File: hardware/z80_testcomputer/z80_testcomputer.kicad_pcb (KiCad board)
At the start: 2 copper layers, 95 x 100 mm, 16 parts, among them J1 Conn_02x15_Odd_Even, J2 Conn_02x15_Odd_Even, U1 Z84C000XVEG, U2 SRAM_512K8B_DIP_SOP_SOJ

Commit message: added EEPROM, experimenting with packages
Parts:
- added C5: 100n, SquantorRcl:C_0805+0603, F.Cu at (225.4, 145.7)
- added C6: 1u, SquantorRcl:C_0805+0603, F.Cu at (243.8, 103.5)
- added U3: EEPROM_512K8B_DIP, Package_DIP:DIP-32_W15.24mm, F.Cu at (224.7, 104.0)
- U2: footprint Package_SO:SSOP-32_11.305x20.495mm_P1.27mm -> Package_DIP:DIP-32_W15.24mm
- moved U2 96.5 mm to (245.0, 133.1)
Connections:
- U2 pad 1: (no net) -> /A17
- U2 pad 2: (no net) -> /A16
- U2 pad 30: (no net) -> /A18
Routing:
- net /!WR: track 62.8 -> 0.00 mm
- net /!BUSACK: track 62.8 -> 0.00 mm
- net /!WAIT: track 62.8 -> 0.00 mm
- net /!RD: track 62.8 -> 0.00 mm
- net /!NMI: track 62.0 -> 0.00 mm
- net /!HALT: track 61.9 -> 0.00 mm
- net /!MREQ: track 61.6 -> 0.00 mm
- net /!IORQ: track 61.6 -> 0.00 mm

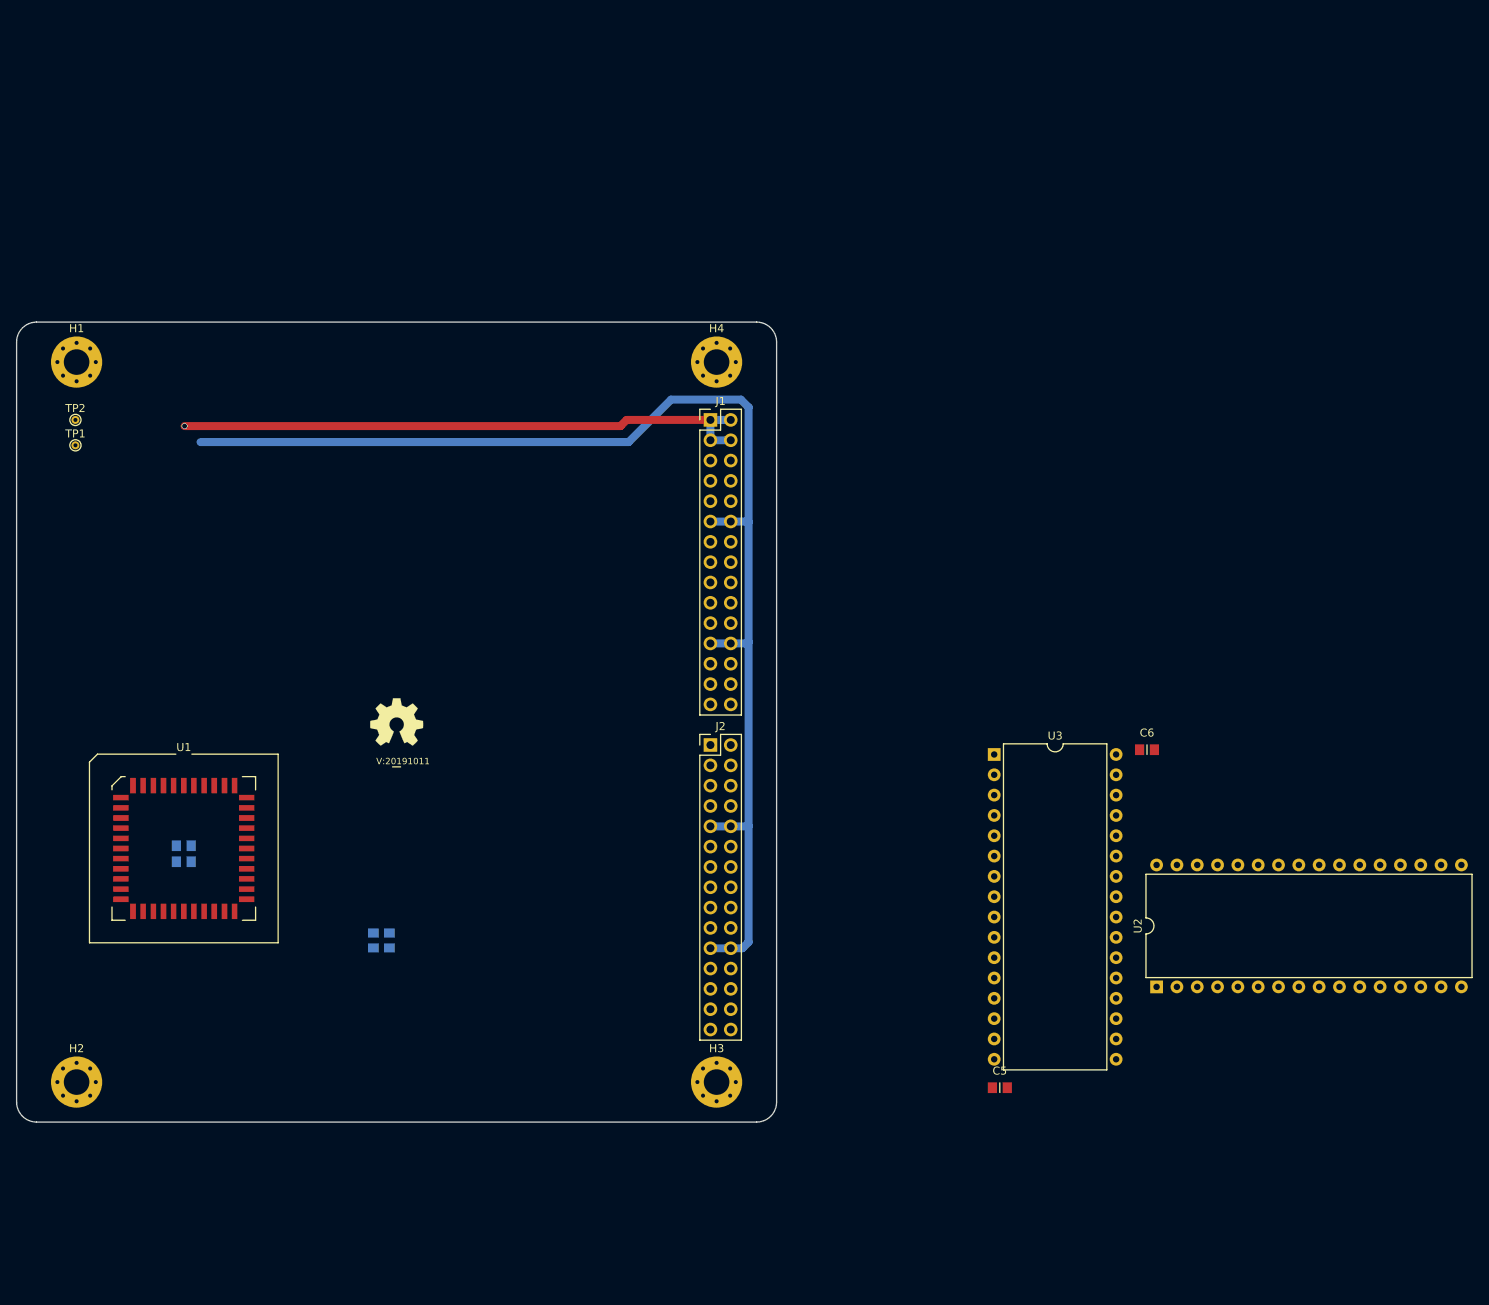
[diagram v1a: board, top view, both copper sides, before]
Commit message: again switched back to PDIP to make a simpler board and easier to route
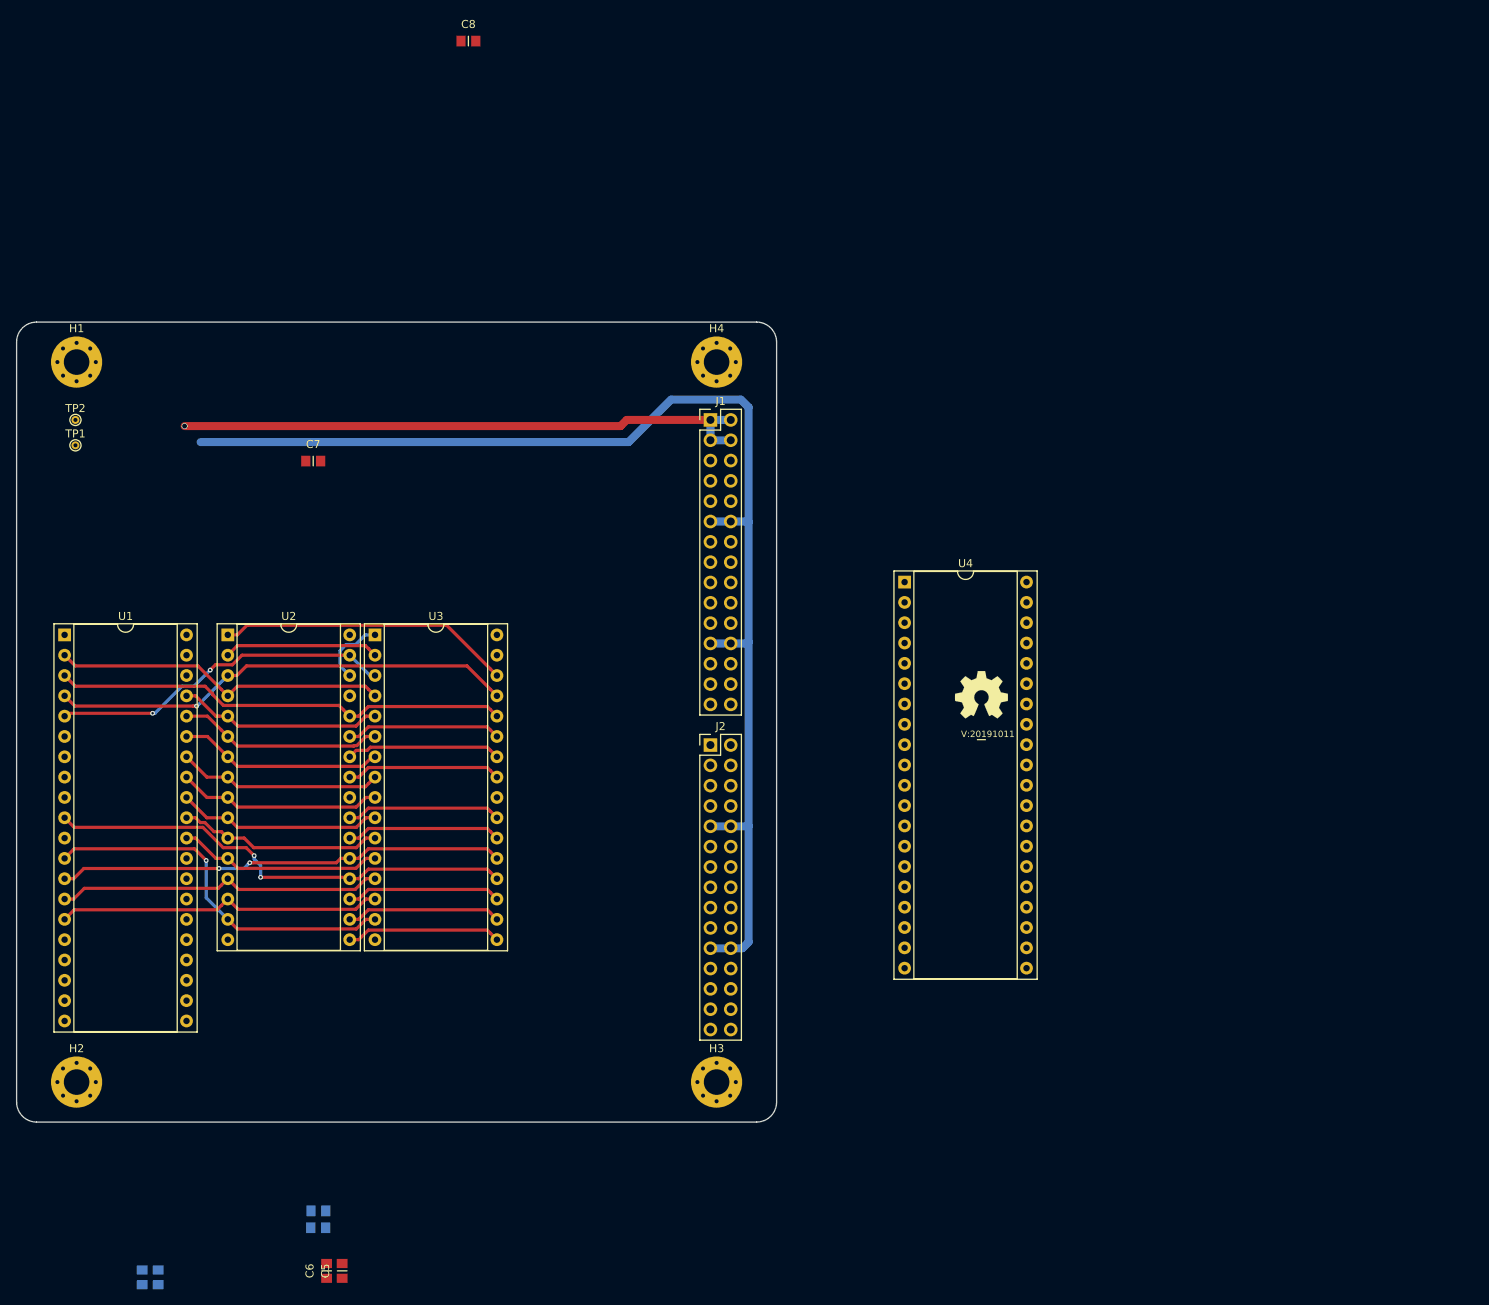
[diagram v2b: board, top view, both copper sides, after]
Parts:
- added C7: 100n, SquantorRcl:C_0805+0603, F.Cu at (139.6, 67.4)
- added C8: 1u, SquantorRcl:C_0805+0603, F.Cu at (159.0, 14.9)
- added U4: Z84C200XPEG, Package_DIP:DIP-40_W15.24mm_Socket, F.Cu at (213.5, 82.5)
- U1: value Z84C000XVEG -> Z84C000XPEG; footprint Package_LCC:PLCC-44_SMD-Socket -> Package_DIP:DIP-40_W15.24mm_Socket
- U2, U3: footprint Package_DIP:DIP-32_W15.24mm -> Package_DIP:DIP-32_W15.24mm_Socket
- moved U2 124.2 mm to (128.9, 89.1), turned to 0 degrees
- moved C6 121.5 mm to (141.2, 168.6), turned to 90 degrees
- moved C5 85.3 mm to (143.2, 168.6), turned to 90 degrees
- moved U3 78.8 mm to (147.3, 89.1)
- moved N1 73.2 mm to (223.1, 96.6)
- moved N2 73.2 mm to (223.1, 101.6)
- moved C3 51.1 mm to (118.2, 169.4)
- moved C4 51.1 mm to (120.2, 169.4)
- moved C2 50.6 mm to (140.2, 163.2)
- moved C1 46.8 mm to (140.2, 161.1)
- moved U1 30.6 mm to (108.5, 89.1)
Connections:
- J1 pad 17: /A11 -> /A15
- J1 pad 18: /A10 -> /A14
- J1 pad 19: /A12 -> /A13
- J1 pad 20: /A9 -> /A12
- J1 pad 21: /A13 -> /A11
- J1 pad 22: /A8 -> /A10
- J1 pad 25: /A14 -> /A9
- J1 pad 26: /A7 -> /A8
- J1 pad 27: /A15 -> /A7
- J1 pad 29: /MCLK -> /A5
- J1 pad 30: /A5 -> /A4
- J2 pad 1: /D4 -> /A3
- J2 pad 11: /D2 -> /!WAIT
- J2 pad 12: /A0 -> /!BUSACK
- J2 pad 13: /D7 -> /!WR
- J2 pad 14: /!RFSH -> /!RD
- J2 pad 15: /D0 -> /!IORQ
- J2 pad 16: /!M1 -> /!MREQ
- J2 pad 17: /D1 -> /!HALT
- J2 pad 18: /!RESET -> /!NMI
- J2 pad 2: /A4 -> /A2
- J2 pad 20: /!BUSREQ -> /D1
- J2 pad 23: /!NMI -> /D0
- J2 pad 24: /!WAIT -> /D7
- J2 pad 25: /!HALT -> /D2
- J2 pad 26: /!BUSACK -> /D6
- J2 pad 27: /!MREQ -> /D5
- J2 pad 28: /!WR -> /D3
- J2 pad 29: /!IORQ -> /D4
- J2 pad 3: /D3 -> /A1
- J2 pad 30: /!RD -> /MCLK
- J2 pad 4: /A3 -> /A0
- J2 pad 5: /D5 -> /!RFSH
- J2 pad 6: /A2 -> /!M1
- J2 pad 7: /D6 -> /!RESET
- J2 pad 8: /A1 -> /!BUSREQ
- U1 pad 10: /D5 -> /D6
- U1 pad 11: /D6 -> /VDD
- U1 pad 12: (no net) -> /D2
- U1 pad 13: /VDD -> /D7
- U1 pad 14: /D2 -> /D0
- U1 pad 15: /D7 -> /D1
- U1 pad 16: /D0 -> /!INT
- U1 pad 17: /D1 -> /!NMI
- U1 pad 18: /!INT -> /!HALT
- U1 pad 19: /!NMI -> /!MREQ
- U1 pad 20: /!HALT -> /!IORQ
- U1 pad 21: /!MREQ -> /!RD
- U1 pad 22: /!IORQ -> /!WR
- U1 pad 23: /!RD -> /!BUSACK
- U1 pad 24: (no net) -> /!WAIT
- U1 pad 25: (no net) -> /!BUSREQ
- U1 pad 26: /!WR -> /!RESET
- U1 pad 27: /!BUSACK -> /!M1
- U1 pad 28: /!WAIT -> /!RFSH
- U1 pad 29: /!BUSREQ -> /VSS
- U1 pad 30: /!RESET -> /A0
- U1 pad 31: /!M1 -> /A1
- U1 pad 32: /!RFSH -> /A2
- U1 pad 33: /VSS -> /A3
- U1 pad 34: /A0 -> /A4
- U1 pad 35: /A1 -> /A5
- U1 pad 36: /A2 -> /A6
- U1 pad 37: /A3 -> /A7
- U1 pad 38: /A4 -> /A8
- U1 pad 39: /A5 -> /A9
- U1 pad 40: /A6 -> /A10
- U1 pad 6: (no net) -> /MCLK
- U1 pad 7: /MCLK -> /D4
- U1 pad 8: /D4 -> /D3
- U1 pad 9: /D3 -> /D5
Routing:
- net /D6: track 0.00 -> 59.3 mm, vias 0 -> 2
- net /A14: track 0.00 -> 58.2 mm, vias 0 -> 1
- net /A13: track 0.00 -> 57.2 mm
- net /D7: track 0.00 -> 56.1 mm, vias 0 -> 2
- net /D2: track 0.00 -> 46.7 mm, vias 0 -> 1
- net /A15: track 0.00 -> 43.0 mm, vias 0 -> 2
- net /A12: track 0.00 -> 41.9 mm
- net /D0: track 0.00 -> 41.0 mm
- net /D1: track 0.00 -> 40.9 mm
- net /A17: track 0.00 -> 36.7 mm
- net /A0: track 0.00 -> 25.6 mm
- net /A7: track 0.00 -> 25.6 mm
- net /A5: track 0.00 -> 25.6 mm
- net /A3: track 0.00 -> 25.6 mm
- net /A1: track 0.00 -> 25.6 mm
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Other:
- net class Default: clearance 0.127 -> 0.2; trace_width 0.127 -> 0.3
- rule trace_clearance: 0.127 -> 0.2

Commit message: added bus testpoints for new layout test
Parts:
- added J3: Conn_01x32, Connector_PinHeader_1.27mm:PinHeader_1x32_P1.27mm_Vertical, F.Cu at (132.1, 94.1)
- moved U2 40.0 mm to (138.0, 128.0), turned to 90 degrees
- moved U3 22.5 mm to (138.0, 109.6), turned to 90 degrees
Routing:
- net /D6: track 59.3 -> 0.00 mm, vias 2 -> 0
- net /A14: track 58.2 -> 0.00 mm, vias 1 -> 0
- net /A13: track 57.2 -> 0.00 mm
- net /D7: track 56.1 -> 0.00 mm, vias 2 -> 0
- net /D2: track 46.7 -> 0.00 mm, vias 1 -> 0
- net /A15: track 43.0 -> 0.00 mm, vias 2 -> 0
- net /A12: track 41.9 -> 0.00 mm
- net /D0: track 41.0 -> 0.00 mm
- net /D1: track 40.9 -> 0.00 mm
- net /A0: track 25.6 -> 0.00 mm
- net /A7: track 25.6 -> 0.00 mm
- net /A5: track 25.6 -> 0.00 mm
- net /A3: track 25.6 -> 0.00 mm
- net /A1: track 25.6 -> 0.00 mm
- net /A4: track 25.6 -> 0.00 mm
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
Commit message: changed pcb rules a bit, added a net class for clock, layed out bus, RAM/ROM combo and added enables
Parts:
- moved C1 53.0 mm to (114.5, 114.7)
- moved C2 53.0 mm to (114.5, 116.8)
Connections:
- J1 pad 17: /A15 -> (no net)
- J1 pad 18: /A14 -> (no net)
- J1 pad 19: /A13 -> (no net)
- J1 pad 20: /A12 -> (no net)
- J1 pad 21: /A11 -> (no net)
- J1 pad 22: /A10 -> (no net)
- J1 pad 25: /A9 -> (no net)
- J1 pad 26: /A8 -> (no net)
- J1 pad 27: /A7 -> (no net)
- J1 pad 28: /A6 -> (no net)
- J1 pad 29: /A5 -> (no net)
- J1 pad 30: /A4 -> (no net)
- J2 pad 1: /A3 -> (no net)
- J2 pad 11: /!WAIT -> (no net)
- J2 pad 12: /!BUSACK -> (no net)
- J2 pad 13: /!WR -> (no net)
- J2 pad 14: /!RD -> (no net)
- J2 pad 15: /!IORQ -> (no net)
- J2 pad 16: /!MREQ -> (no net)
- J2 pad 17: /!HALT -> (no net)
- J2 pad 18: /!NMI -> (no net)
- J2 pad 19: /!INT -> (no net)
- J2 pad 2: /A2 -> (no net)
- J2 pad 20: /D1 -> (no net)
- J2 pad 23: /D0 -> (no net)
- J2 pad 24: /D7 -> (no net)
- J2 pad 25: /D2 -> (no net)
- J2 pad 26: /D6 -> (no net)
- J2 pad 27: /D5 -> (no net)
- J2 pad 28: /D3 -> (no net)
- J2 pad 29: /D4 -> (no net)
- J2 pad 3: /A1 -> (no net)
- J2 pad 30: /MCLK -> (no net)
- J2 pad 4: /A0 -> (no net)
- J2 pad 5: /!RFSH -> (no net)
- J2 pad 6: /!M1 -> (no net)
- J2 pad 7: /!RESET -> (no net)
- J2 pad 8: /!BUSREQ -> (no net)
- J3 pad 1: (no net) -> /A11
- J3 pad 10: (no net) -> /A6
- J3 pad 11: (no net) -> /A5
- J3 pad 12: (no net) -> /A4
- J3 pad 13: (no net) -> /A3
- J3 pad 14: (no net) -> /A2
- J3 pad 15: (no net) -> /A1
- J3 pad 16: (no net) -> /A0
- J3 pad 17: (no net) -> /D7
- J3 pad 18: (no net) -> /D6
- J3 pad 19: (no net) -> /D5
- J3 pad 2: (no net) -> /A12
- J3 pad 20: (no net) -> /D4
- J3 pad 21: (no net) -> /D3
- J3 pad 22: (no net) -> /D2
- J3 pad 23: (no net) -> /D1
- J3 pad 24: (no net) -> /D0
- J3 pad 25: (no net) -> /!M1
- J3 pad 26: (no net) -> /!RESET
- J3 pad 27: (no net) -> /!INT
- J3 pad 28: (no net) -> /!MREQ
- J3 pad 29: (no net) -> /!WR
- J3 pad 3: (no net) -> /A13
- J3 pad 30: (no net) -> /!IORQ
- J3 pad 31: (no net) -> /!RD
- J3 pad 32: (no net) -> /MCLK
- J3 pad 4: (no net) -> /A14
- J3 pad 5: (no net) -> /A15
- J3 pad 6: (no net) -> /A10
- J3 pad 7: (no net) -> /A9
- J3 pad 8: (no net) -> /A8
- J3 pad 9: (no net) -> /A7
- U1 pad 17: /!NMI -> (no net)
- U1 pad 18: /!HALT -> (no net)
- U1 pad 23: /!BUSACK -> (no net)
- U1 pad 24: /!WAIT -> (no net)
- U1 pad 25: /!BUSREQ -> (no net)
- U1 pad 28: /!RFSH -> (no net)
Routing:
- net /MCLK: track 0.00 -> 66.4 mm
- net /VDD: track 73.7 -> 12.8 mm, vias 1 -> 0
- net /VSS: track 157.5 -> 112.4 mm
- net /D4: track 19.4 -> 53.7 mm, vias 0 -> 1
- net /D3: track 19.4 -> 52.1 mm, vias 0 -> 1
- net /D6: track 0.00 -> 29.8 mm, vias 0 -> 1
- net /D5: track 19.4 -> 46.1 mm, vias 0 -> 1
- net /!MREQ: track 0.00 -> 26.3 mm
- net /!IORQ: track 0.00 -> 26.3 mm
- net /D7: track 0.00 -> 25.7 mm, vias 0 -> 1
- net /A11: track 19.4 -> 45.1 mm, vias 0 -> 1
- net /A12: track 0.00 -> 25.1 mm, vias 0 -> 1
- net /D2: track 0.00 -> 25.1 mm
- net /D1: track 0.00 -> 25.1 mm, vias 0 -> 1
- net /A15: track 0.00 -> 24.7 mm, vias 0 -> 1
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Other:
- net class CLK added: clearance 0.4, trace_width 0.4, via_dia 0.6, via_drill 0.4
- net class Default: trace_width 0.3 -> 0.2

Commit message: further layout of RAM/ROM, bus seems good enough
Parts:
- C5, C6: moved to B.Cu
- moved C5 68.4 mm to (158.1, 101.8)
- moved C6 68.4 mm to (156.2, 101.8)
- moved C3 62.0 mm to (156.0, 120.2)
- moved C4 62.0 mm to (158.0, 120.2)
- moved J3 3.40 mm to (128.7, 94.1)
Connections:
- U2 pad 24: (no net) -> /!MEM_RD
- U2 pad 29: (no net) -> /!MEM_WR
- U3 pad 24: (no net) -> /!MEM_RD
- U3 pad 31: (no net) -> /!MEM_WR
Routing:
- net /VDD: track 12.8 -> 126.0 mm, vias 0 -> 2
- net /VSS: track 112.4 -> 192.7 mm, vias 0 -> 4
- net /A17: track 36.7 -> 0.00 mm
- net /A13: track 24.6 -> 60.4 mm, vias 1 -> 2
- net /A10: track 34.2 -> 65.9 mm, vias 0 -> 1
- net /A12: track 25.1 -> 52.7 mm, vias 1 -> 2
- net /A11: track 45.1 -> 70.5 mm, vias 1 -> 2
- net /A15: track 24.7 -> 46.7 mm, vias 1 -> 2
- net /D6: track 29.8 -> 49.3 mm
- net /!MEM_RD: track 0.00 -> 19.5 mm
- net (no net): track 19.4 -> 0.00 mm
- net /A16: track 19.4 -> 0.00 mm
- net /D1: track 25.1 -> 43.3 mm
- net /D7: track 25.7 -> 43.2 mm
- net /A14: track 24.3 -> 40.6 mm, vias 1 -> 2
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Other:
- net class PWR added: clearance 0.3, trace_width 0.6, via_dia 0.8, via_drill 0.6

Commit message: some power distribution routing
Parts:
- moved C7 96.4 mm to (224.6, 112.9)
- moved TP2 10.5 mm to (106.0, 72.0)
- moved TP1 6.00 mm to (106.0, 70.0)
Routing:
- net /VDD: track 126.0 -> 273.7 mm, vias 2 -> 3
- net /VSS: track 192.7 -> 330.1 mm, vias 4 -> 5
- net /A4: track 7.38 -> 58.7 mm, vias 0 -> 1
- net /A5: track 8.40 -> 57.7 mm, vias 0 -> 1
- net /A6: track 9.42 -> 56.8 mm, vias 0 -> 1
- net /A7: track 10.6 -> 56.2 mm, vias 0 -> 1
- net /A14: track 40.6 -> 71.4 mm, vias 2 -> 4
- net /A9: track 32.3 -> 57.5 mm, vias 0 -> 1
- net /A8: track 31.1 -> 53.6 mm, vias 0 -> 1
- net /A1: track 4.99 -> 24.5 mm
- net /A3: track 6.37 -> 25.8 mm
- net /A12: track 52.7 -> 72.2 mm
- net /A2: track 5.45 -> 24.9 mm
- net /D2: track 24.7 -> 41.2 mm
- net /A18: track 0.00 -> 9.02 mm
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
